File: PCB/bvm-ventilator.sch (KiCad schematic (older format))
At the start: 0 parts

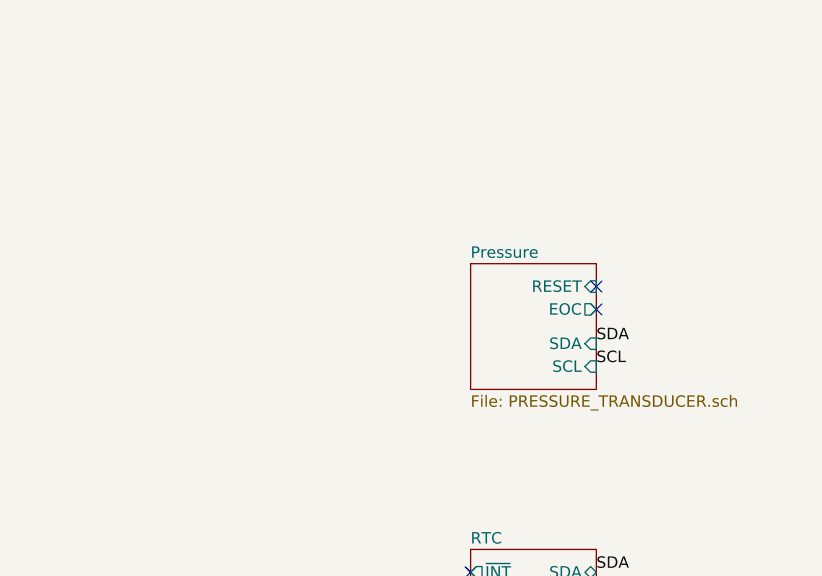
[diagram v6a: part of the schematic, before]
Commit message: Added differential pressure and level shifter for gauge pressure sensor
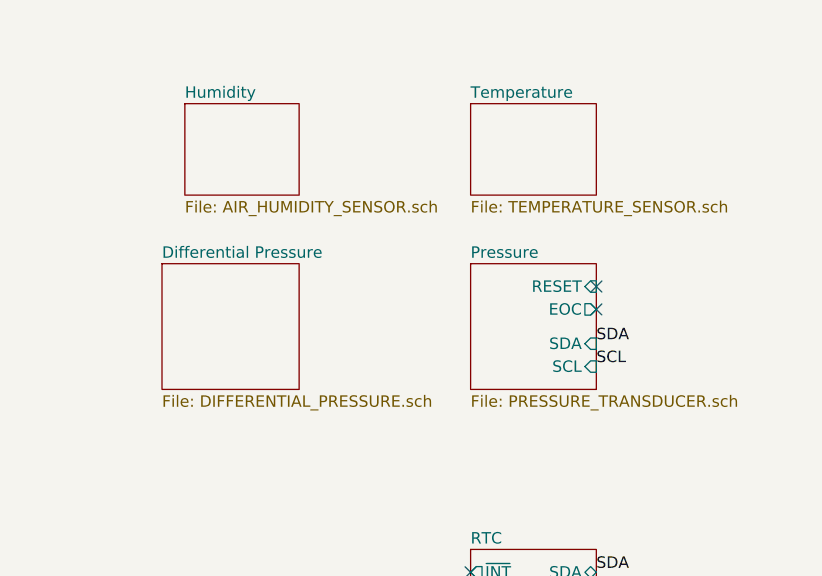
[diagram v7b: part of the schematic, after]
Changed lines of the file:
@@
 $Descr A4 11693 8268
 encoding utf-8
-Sheet 1 21
+Sheet 1 25
 Title "BVM Ventilator"
 Date ""
@@
 Text Label 6250 3500 0    50   ~ 0
 LINEAR_ENCODER_B
+$Sheet
+S 9900 1000 550  400
+U 5E8D66CB
+F0 "Temperature" 50
+F1 "TEMPERATURE_SENSOR.sch" 50
+$EndSheet
+$Sheet
+S 8650 1000 500  400
+U 5E8D6DCE
+F0 "Humidity" 50
+F1 "AIR_HUMIDITY_SENSOR.sch" 50
+$EndSheet
+$Sheet
+S 8550 1700 600  550
+U 5E8D7701
+F0 "Differential Pressure" 50
+F1 "DIFFERENTIAL_PRESSURE.sch" 50
+$EndSheet
 $EndSCHEMATC

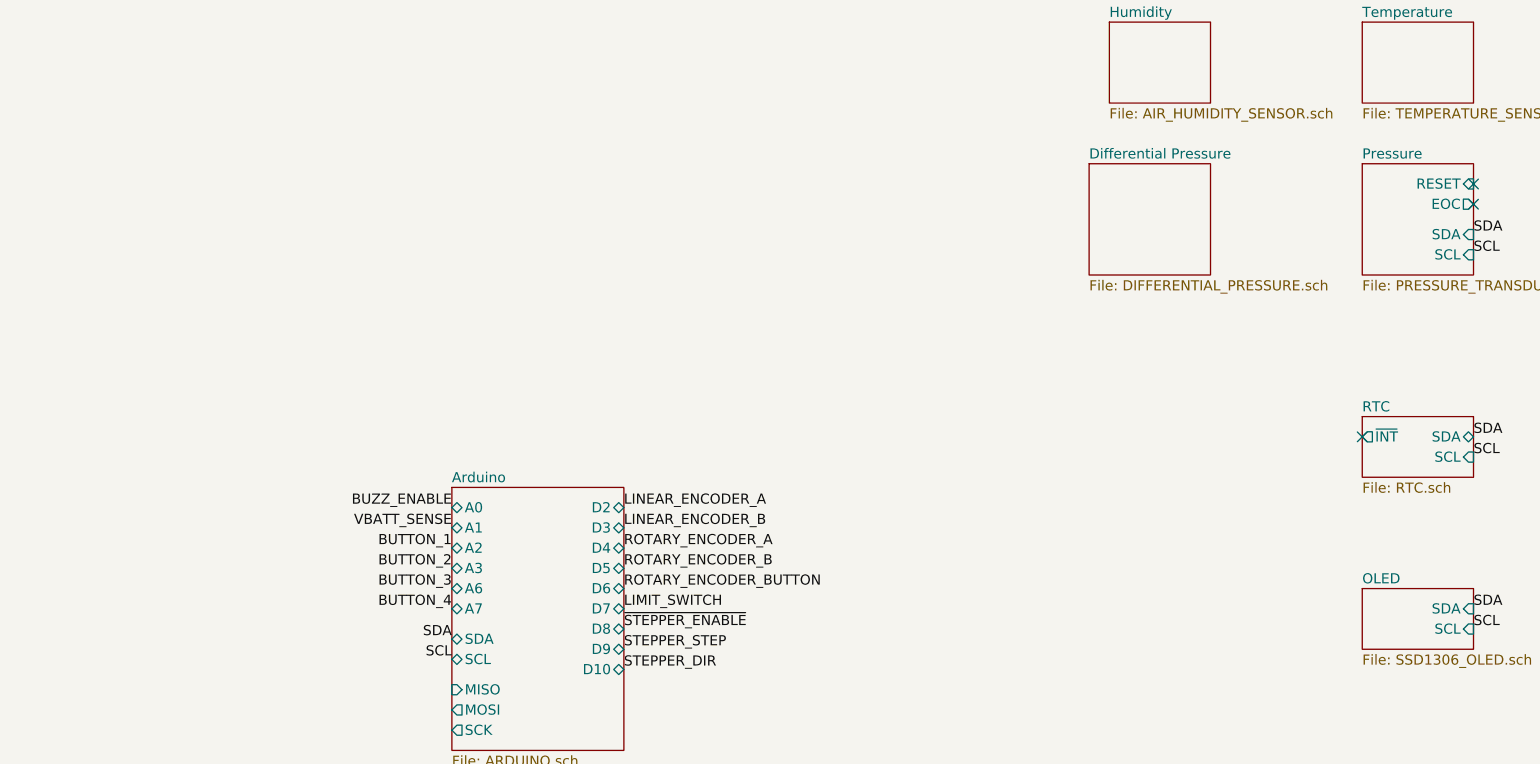
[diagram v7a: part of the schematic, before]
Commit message: Connected Differential pressure sensor
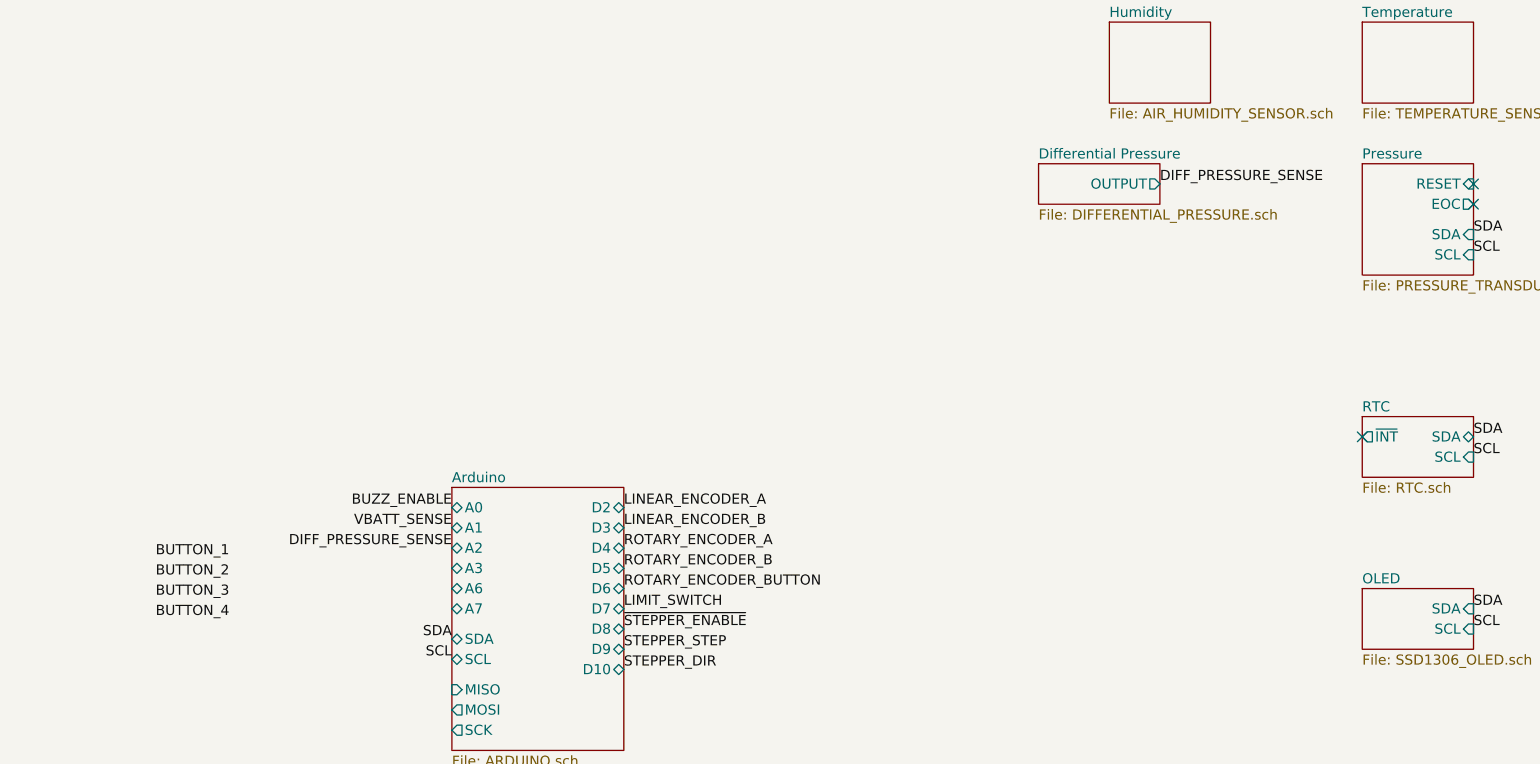
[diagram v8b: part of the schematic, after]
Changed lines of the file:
@@
 Text Label 8650 6200 0    50   ~ 0
 BUTTON_3
-Text Label 5400 3600 2    50   ~ 0
+Text Label 4300 3650 2    50   ~ 0
 BUTTON_1
-Text Label 5400 3800 2    50   ~ 0
+Text Label 4300 3850 2    50   ~ 0
 BUTTON_3
-Text Label 5400 3700 2    50   ~ 0
+Text Label 4300 3750 2    50   ~ 0
 BUTTON_2
-Text Label 5400 3900 2    50   ~ 0
+Text Label 4300 3950 2    50   ~ 0
 BUTTON_4
 Text Label 2200 5250 0    50   ~ 0
@@
 $EndSheet
 $Sheet
-S 8550 1700 600  550
+S 8300 1700 600  200
 U 5E8D7701
 F0 "Differential Pressure" 50
 F1 "DIFFERENTIAL_PRESSURE.sch" 50
+F2 "OUTPUT" O R 8900 1800 50
 $EndSheet
+Text Label 8900 1800 0    50   ~ 0
+DIFF_PRESSURE_SENSE
+Text Label 5400 3600 2    50   ~ 0
+DIFF_PRESSURE_SENSE
 $EndSCHEMATC
